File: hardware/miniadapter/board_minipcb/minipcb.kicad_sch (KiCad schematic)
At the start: 22 parts, among them Q102 FDG1024NZ, U102 SN74LVC1G14DRL, U103 TPS62933P

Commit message: new layout
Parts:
- added H108, H109, H110, H111: Pad, Connector_Wire:SolderWirePad_1x01_SMD_1.5x3mm, symbol Mechanical:MountingHole_Pad
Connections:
- net +3V3: now also H106.1, H108.1; no longer H104.1
- net GND: now also H107.1, H111.1; no longer H106.1
- net IO4: now also H104.1, H110.1; no longer H105.1
- net IO5: now also H105.1, H109.1; no longer H107.1
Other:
- moved on the sheet: H104, H105, H106, H107

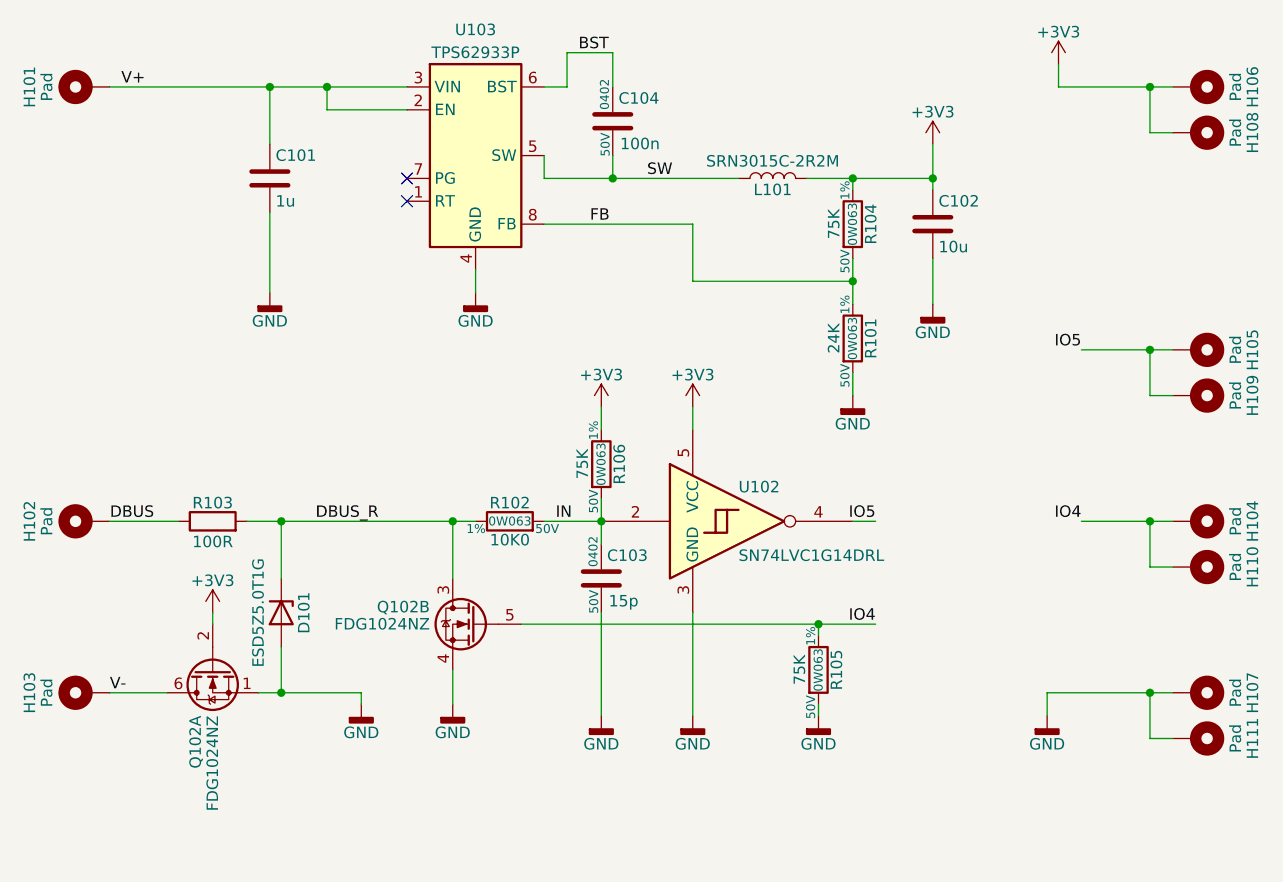
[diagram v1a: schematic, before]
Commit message: layout changes and panel generation
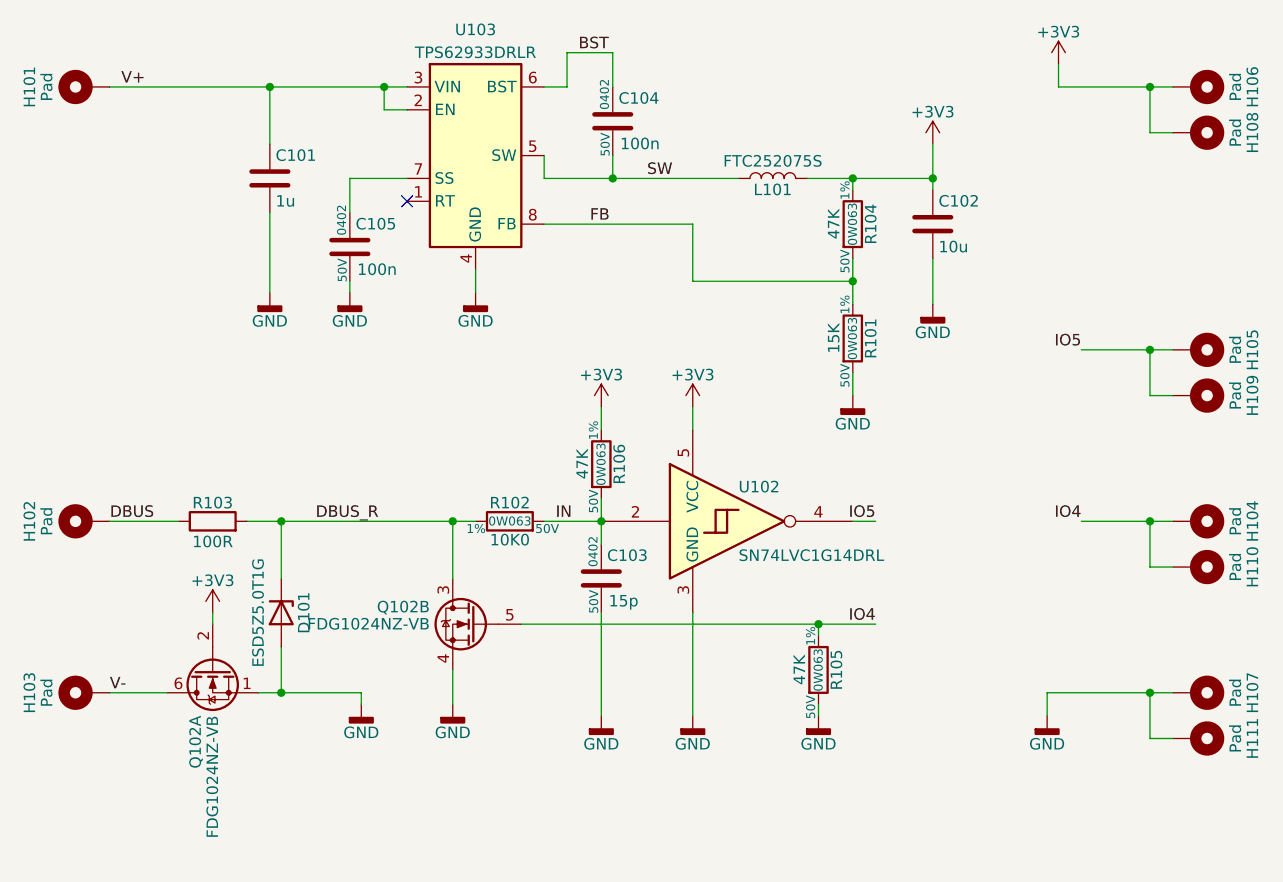
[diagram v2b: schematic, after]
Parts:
- removed U103: TPS62933P, Package_TO_SOT_SMD:SOT-583-8, symbol Regulator_Switching:TPS62933P
- added C105: C_100n_0402_X7R_10%_50V, Capacitor_SMD:C_0402_1005Metric, symbol 900_capacitors:C_100n_0402_X7R_10%_50V
- added U103: TPS62933DRLR, Package_TO_SOT_SMD:SOT-583-8, symbol Regulator_Switching:TPS62933F
- C101: OC_JLCPCB (none) -> C15849
- C102: OC_JLCPCB (none) -> C19702
- C103: OC_JLCPCB (none) -> C1548
- C104: OC_JLCPCB (none) -> C307331
- D101: OC_JLCPCB (none) -> C3008120
- H101, H102, H103: OC_JLCPCB (none) -> C5334114; now in the parts list
- L101: value SRN3015C-2R2M -> FTC252075S; footprint Inductor_SMD:L_Coilcraft_LPS3010 -> Inductor_SMD:L_Changjiang_FTC252075S; OC_JLCPCB (none) -> C5832372
- Q102: value FDG1024NZ -> FDG1024NZ-VB; OC_JLCPCB (none) -> C693215
- R101: value R_24K0_0402_0W063_1%_100PPM_50V -> R_15K_0402_0W063_1%_100PPM_50V; symbol 900_resistors:R_10K0_0402_0W063_1%_100PPM_50V -> 900_resistors:R_15K_0402_0W063_1%_100PPM_50V; ID 50000005 -> 50000013; MC_Generic RC0402FR-0710KL -> RC0402FR-0715KL; NAME R_10K0_0402_0W063_1%_100PPM_50V -> R_15K_0402_0W063_1%_100PPM_50V; OC_JLCPCB C60490 -> C25756; OC_MOUSER 603-RC0402FR-0710KL -> 603-RC0402FR-0715KL; Resistance 24K -> 15K; kicadlibid 5 -> 13
- R102: OC_JLCPCB C60490 -> C25744
- R103: OC_JLCPCB (none) -> C22775
- R104, R105, R106: value R_75K_0402_0W063_1%_100PPM_50V -> R_47K_0402_0W063_1%_100PPM_50V; symbol 900_resistors:R_33K_0402_0W063_1%_100PPM_50V -> 900_resistors:R_47K_0402_0W063_1%_100PPM_50V; ID 50000037 -> 50000047; MC_Generic RC0402FR-0733KL -> RC0402FR-0747KL; NAME R_75K_0402_0W063_1%_100PPM_50V -> R_47K_0402_0W063_1%_100PPM_50V; OC_JLCPCB C138003 -> C25792; OC_MOUSER 603-RC0402FR-0733KL -> 603-RC0402FR-0747KL; Resistance 75K -> 47K; kicadlibid 37 -> 47
- U102: OC_JLCPCB (none) -> C19829622
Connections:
- net BST: now also U103.6 (BST)
- net FB: now also U103.8 (FB)
- net GND: now also C105.2, U103.4 (GND)
- net SW: now also U103.5 (SW)
- net V+: now also U103.2 (EN), U103.3 (VIN)
- new net: C105.1, U103.7 (SS)
- no-connect marks 2 -> 1
